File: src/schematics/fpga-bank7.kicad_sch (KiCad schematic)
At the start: 7 parts

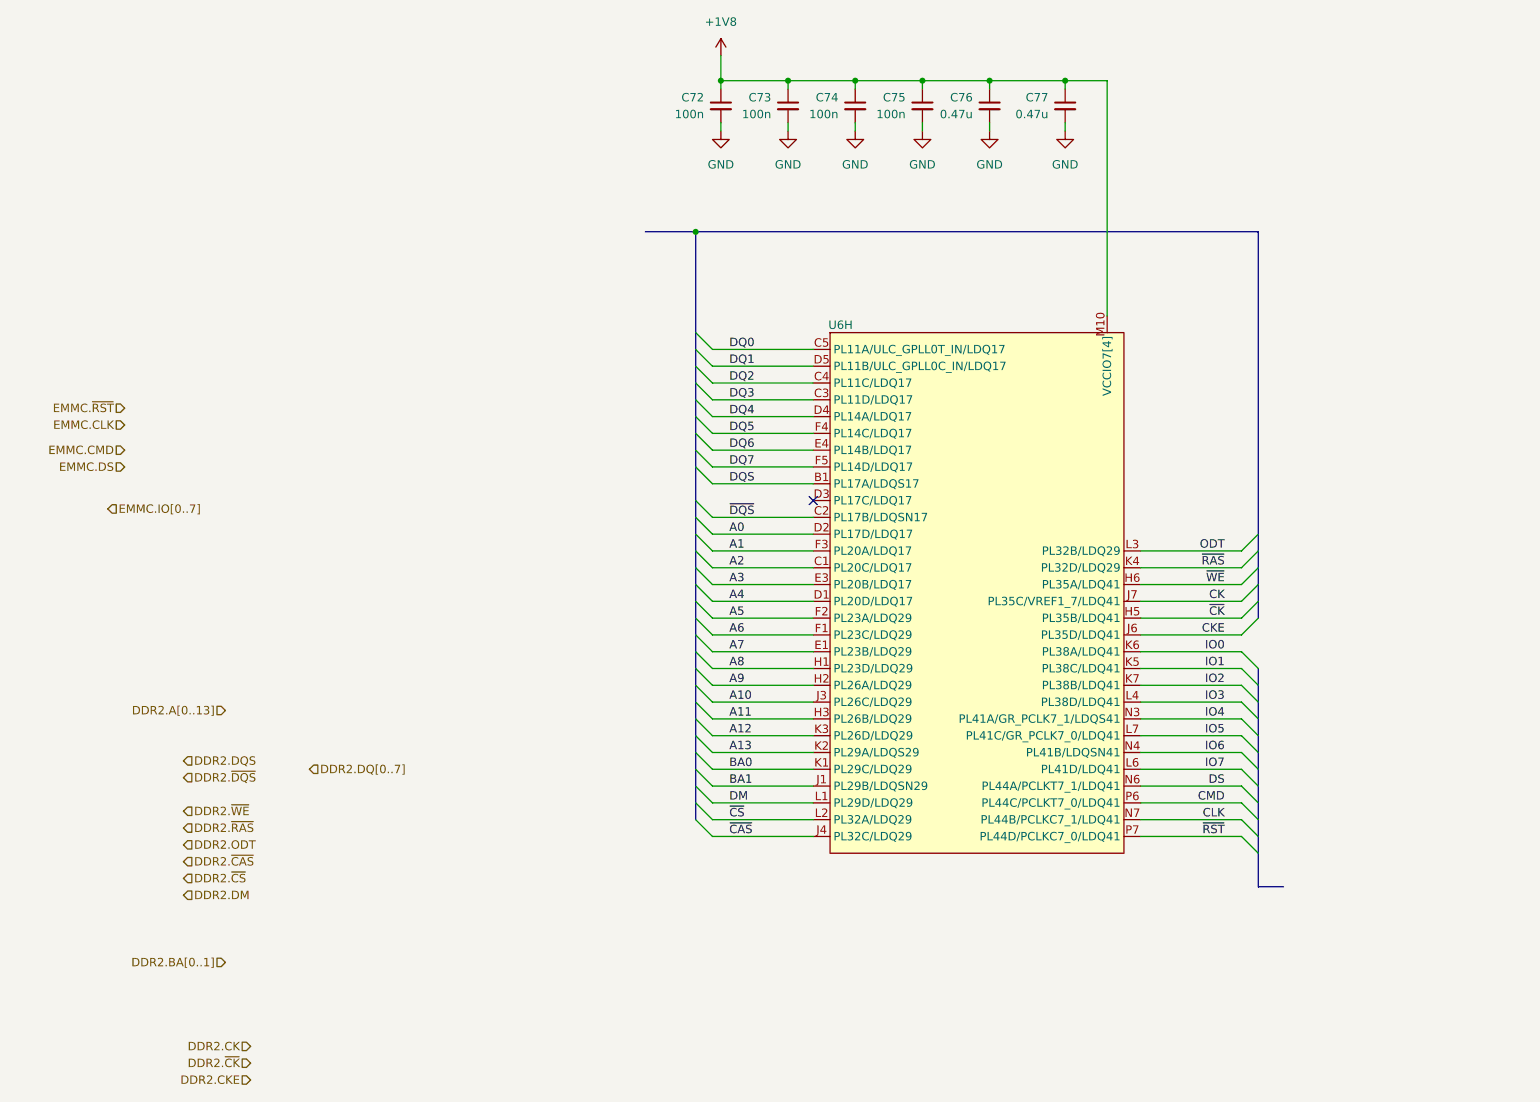
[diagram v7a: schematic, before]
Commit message: Adds a revision history table
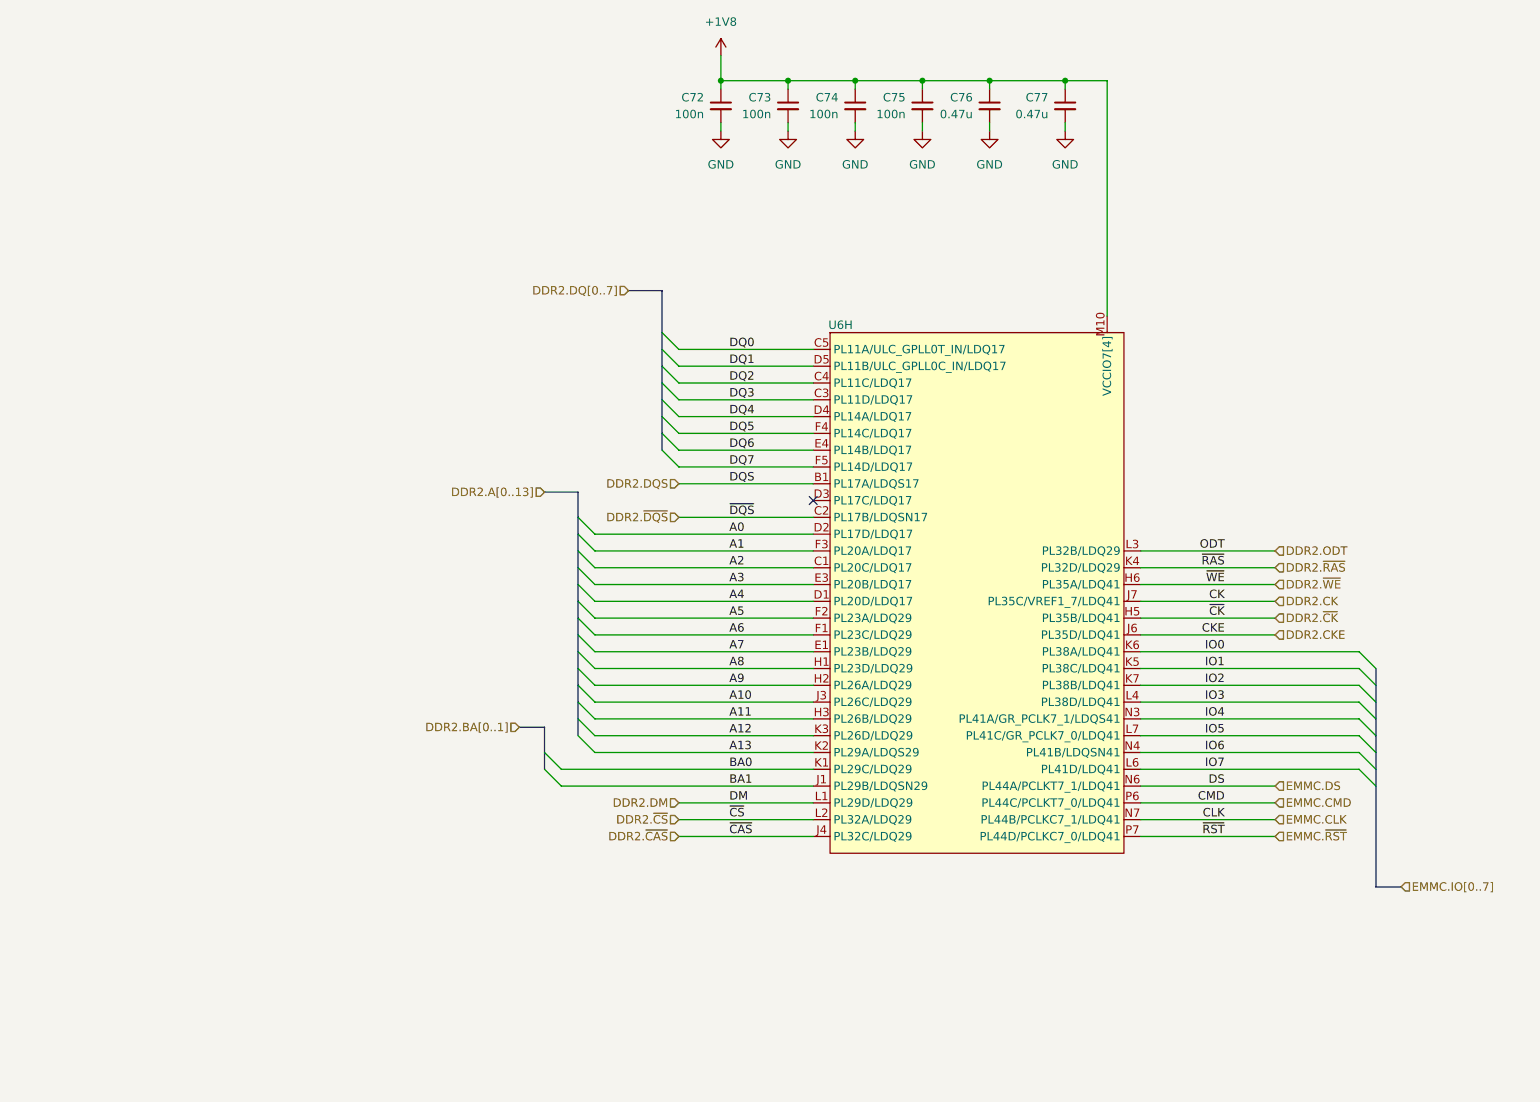
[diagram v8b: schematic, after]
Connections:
- net CK is gone; now on net DDR2.CK: U6.J7 (PL35C/VREF1_7/LDQ41)
- net CKE is gone; now on net DDR2.CKE: U6.J6 (PL35D/LDQ41)
- net CLK is gone; now on net EMMC.CLK: U6.N7 (PL44B/PCLKC7_1/LDQ41)
- net CMD is gone; now on net EMMC.CMD: U6.P6 (PL44C/PCLKT7_0/LDQ41)
- net DM is gone; now on net DDR2.DM: U6.L1 (PL29D/LDQ29)
- net DQS is gone; now on net DDR2.DQS: U6.B1 (PL17A/LDQS17)
- net DS is gone; now on net EMMC.DS: U6.N6 (PL44A/PCLKT7_1/LDQ41)
- net ODT is gone; now on net DDR2.ODT: U6.L3 (PL32B/LDQ29)
- net ~{CAS} is gone; now on net DDR2.~{CAS}: U6.J4 (PL32C/LDQ29)
- net ~{CK} is gone; now on net DDR2.~{CK}: U6.H5 (PL35B/LDQ41)
- net ~{CS} is gone; now on net DDR2.~{CS}: U6.L2 (PL32A/LDQ29)
- net ~{DQS} is gone; now on net DDR2.~{DQS}: U6.C2 (PL17B/LDQSN17)
- net ~{RAS} is gone; now on net DDR2.~{RAS}: U6.K4 (PL32D/LDQ29)
- net ~{RST} is gone; now on net EMMC.~{RST}: U6.P7 (PL44D/PCLKC7_0/LDQ41)
- net ~{WE} is gone; now on net DDR2.~{WE}: U6.H6 (PL35A/LDQ41)
